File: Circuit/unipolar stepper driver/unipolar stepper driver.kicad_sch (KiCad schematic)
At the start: 21 parts, among them Q1 S8050, Q2 S8050, Q3 S8050, Q4 S8050

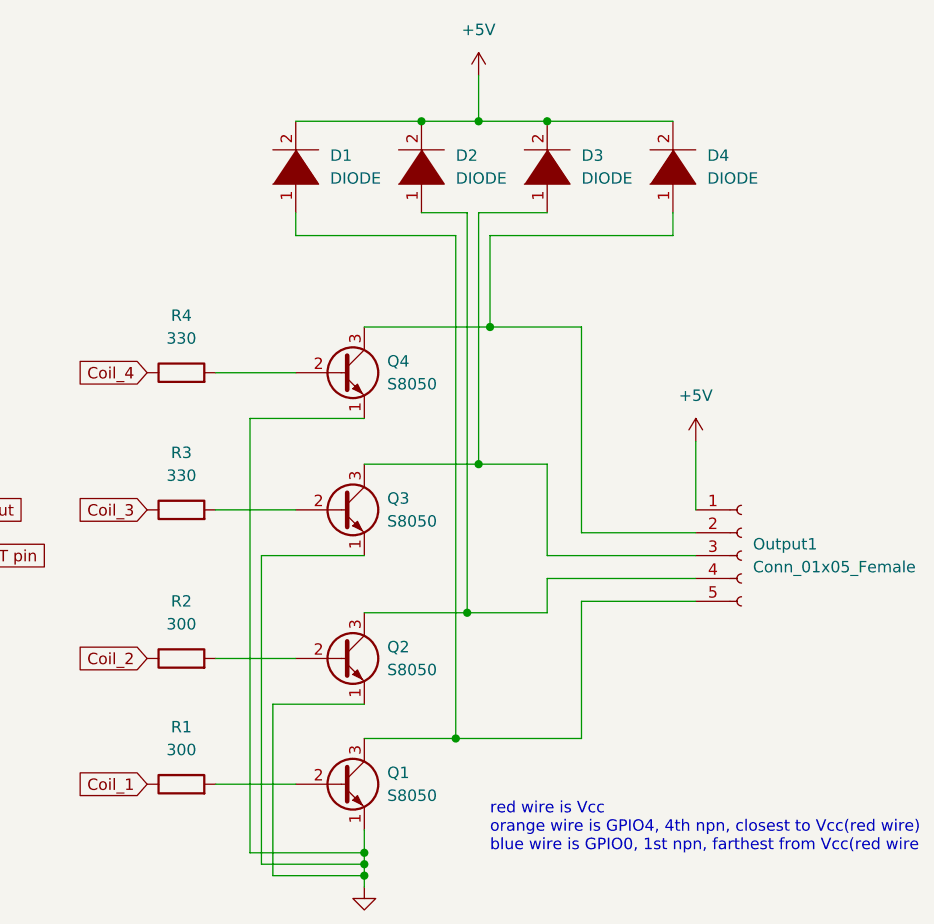
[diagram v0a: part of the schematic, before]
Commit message: Fixed diode directions in unipolar_driver circuit
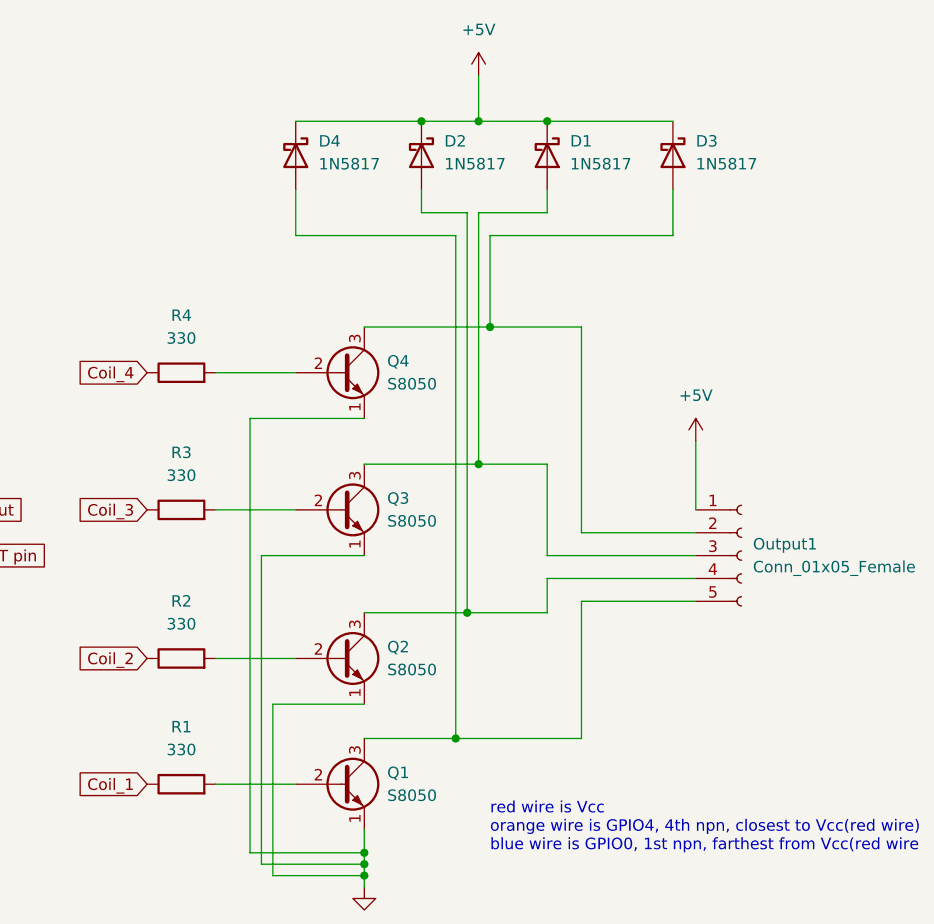
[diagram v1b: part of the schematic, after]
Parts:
- removed D1, D2, D3, D4: DIODE, Diode_THT:D_DO-34_SOD68_P7.62mm_Horizontal, symbol pspice:DIODE
- added D1, D2, D3, D4: 1N5817, Diode_THT:D_DO-34_SOD68_P7.62mm_Horizontal, symbol Diode:1N5817
- R1, R2: value 300 -> 330
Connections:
- net +5V: now also D1.1 (K), D2.1 (K), D3.1 (K), D4.1 (K)
- net at Output1.5 (Pin_5), Q1.3 (C): now also D4.2 (A)
- net at Output1.4 (Pin_4), Q2.3 (C): now also D2.2 (A)
- net at Output1.2 (Pin_2), Q4.3 (C): now also D3.2 (A)
- net at Output1.3 (Pin_3), Q3.3 (C): now also D1.2 (A)

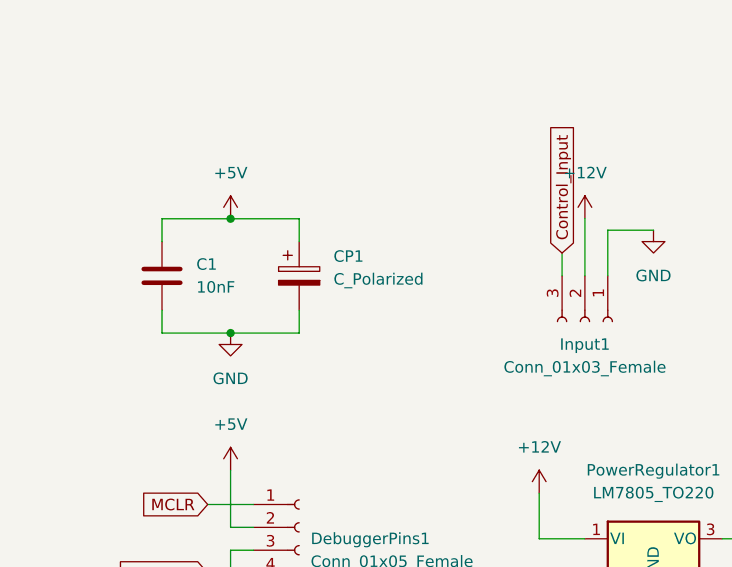
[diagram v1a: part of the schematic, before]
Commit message: looks like CAM module needs bug fixing again
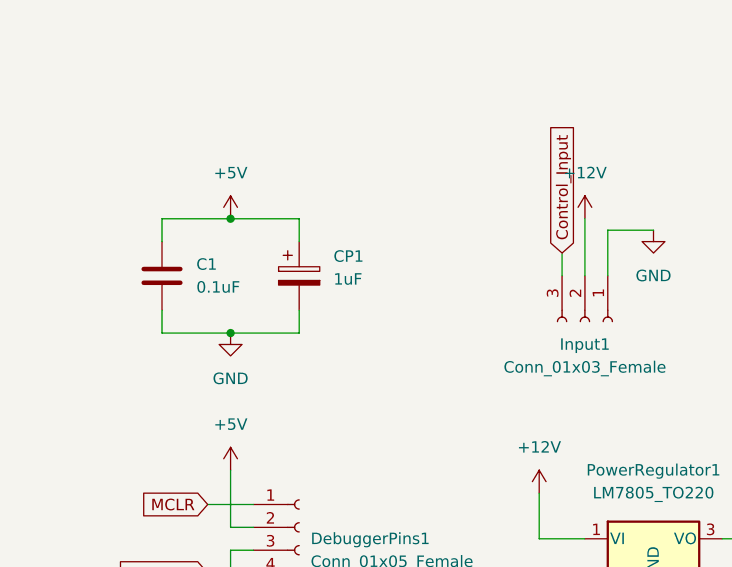
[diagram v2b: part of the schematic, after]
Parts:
- C1: value 10nF -> 0.1uF
- CP1: value C_Polarized -> 1uF
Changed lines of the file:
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@@
       (effects (font (size 1.27 1.27)) (justify right))
     )
-    (property "Value" "10nF" (at 45.72 91.4399 0)
+    (property "Value" "0.1uF" (at 45.72 91.4399 0)
       (effects (font (size 1.27 1.27)) (justify right))
     )
@@
       (effects (font (size 1.27 1.27)) (justify left))
     )
-    (property "Value" "C_Polarized" (at 60.96 90.5509 0)
-      (effects (font (size 1.27 1.27)) (justify left))
-    )
+    (property "Value" "1uF" (at 60.96 90.5509 0)
+      (effects (font (size 1.27 1.27)) (justify left))
+    )
